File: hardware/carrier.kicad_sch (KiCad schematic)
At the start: 49 parts, among them J2 Heltec_J2, J3 Heltec_J3, U2 TCA9534PWR, U3 NS4168

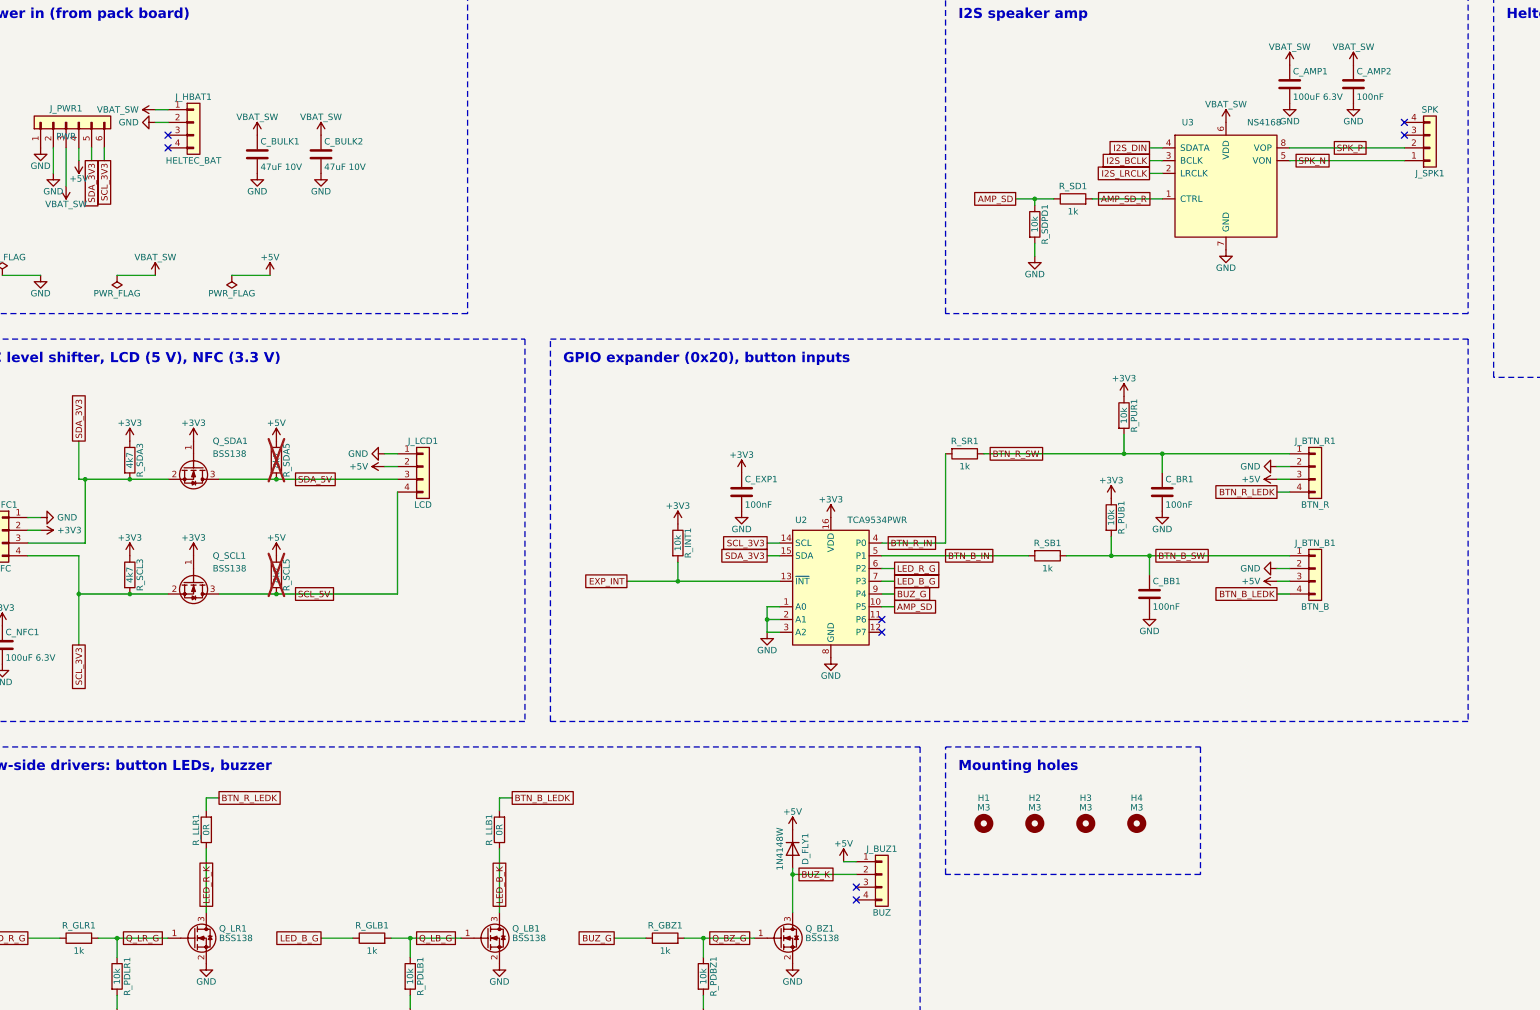
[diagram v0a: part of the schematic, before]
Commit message: hardware: off-board 2-wire connectors back to XH-2
J_HBAT1, J_BUZ1 and J_SPK1 (carrier) and J_KEY1 (pack) go back to JST-XH B2B-XH-A (C158012) instead of 4-pin B4B-XH-A (C144395) with pins 3-4 left no-connect. XH_SPARE is gone from both boards; the freed width puts J_BTN_R1 back on the carrier's top edge. Regenerated: both boards ERC/DRC clean, 0 unrouted.
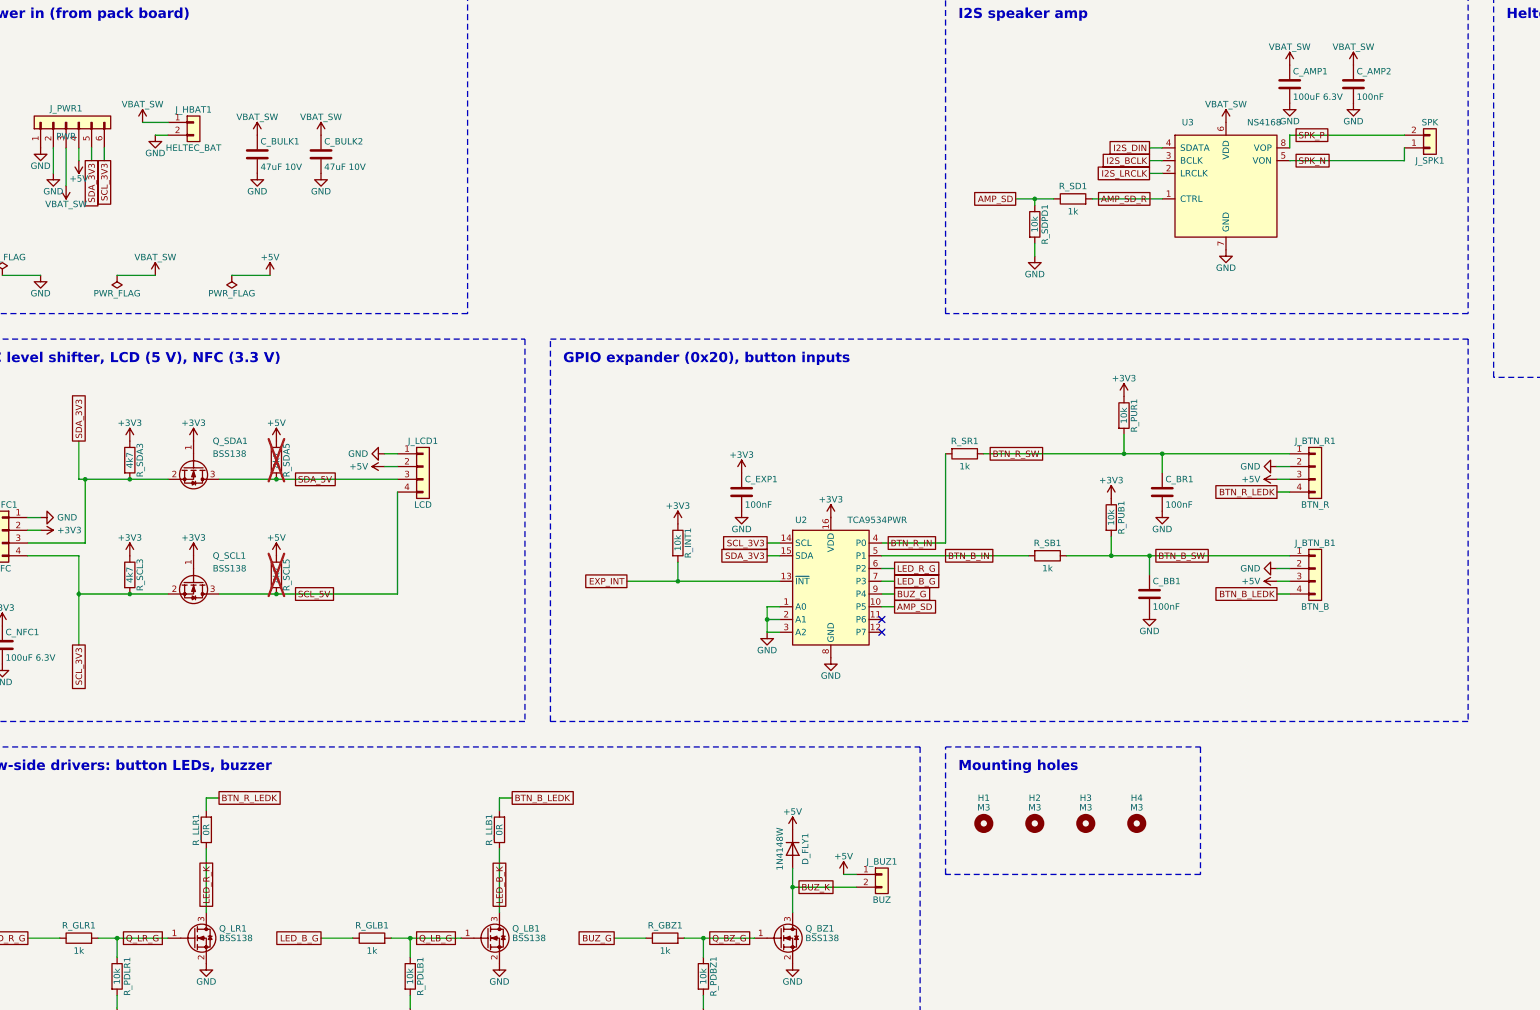
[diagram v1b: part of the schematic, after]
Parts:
- J_BUZ1, J_HBAT1, J_SPK1: footprint Connector_JST:JST_XH_B4B-XH-A_1x04_P2.50mm_Vertical -> Connector_JST:JST_XH_B2B-XH-A_1x02_P2.50mm_Vertical; symbol Connector_Generic:Conn_01x04 -> Connector_Generic:Conn_01x02
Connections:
- no-connect marks 34 -> 28
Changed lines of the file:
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@@
 	(wire
 		(pts
-			(xy 187.96 185.42)
-			(xy 190.5 185.42)
+			(xy 187.96 187.96)
+			(xy 190.5 187.96)
 		)
 		(stroke
@@
 	(wire
 		(pts
-			(xy 177.8 187.96)
-			(xy 190.5 187.96)
+			(xy 177.8 190.5)
+			(xy 190.5 190.5)
 		)
 		(stroke
@@
 		(pts
 			(xy 177.8 186.69)
-			(xy 177.8 187.96)
+			(xy 177.8 190.5)
 		)
 		(stroke
@@
 	(wire
 		(pts
-			(xy 177.8 187.96)
+			(xy 177.8 190.5)
 			(xy 177.8 195.58)
 		)
@@
 	)
 	(junction
-		(at 177.8 187.96)
+		(at 177.8 190.5)
 		(diameter 0)
 		(color 0 0 0 0)
@@
 	(wire
 		(pts
-			(xy 50.8 38.1)
-			(xy 53.34 38.1)
+			(xy 50.8 40.64)
+			(xy 53.34 40.64)
 		)
 		(stroke
@@
 	(wire
 		(pts
-			(xy 276.86 43.18)
 			(xy 299.72 43.18)
+			(xy 299.72 45.72)
 		)
 		(stroke
@@
 	(wire
 		(pts
-			(xy 50.8 35.56)
-			(xy 53.34 35.56)
+			(xy 276.86 40.64)
+			(xy 299.72 40.64)
+		)
+		(stroke
+			(width 0)
+			(type default)
+		)
+	)
+	(wire
+		(pts
+			(xy 276.86 40.64)
+			(xy 276.86 43.18)
+		)
+		(stroke
+			(width 0)
+			(type default)
+		)
+	)
+	(wire
+		(pts
+			(xy 48.26 38.1)
+			(xy 53.34 38.1)
 		)
 		(stroke
@@
 		)
 	)
-	(no_connect
-		(at 53.34 40.64)
-	)
-	(no_connect
-		(at 53.34 43.18)
-	)
 	(rectangle
 		(start 208.28 12.7)
@@
 		)
 	)
-	(no_connect
-		(at 299.72 40.64)
-	)
-	(no_connect
-		(at 299.72 38.1)
-	)
 	(rectangle
 		(start 317.5 12.7)
@@
 		)
 	)
-	(no_connect
-		(at 190.5 190.5)
-	)
-	(no_connect
-		(at 190.5 193.04)
-	)
 	(rectangle
 		(start 208.28 162.56)
@@
 	(global_label "SPK_P"
 		(shape passive)
-		(at 285.75 43.18 0)
+		(at 278.13 40.64 0)
 		(fields_autoplaced yes)
 		(effects
@@
 	(global_label "BUZ_K"
 		(shape passive)
-		(at 179.07 187.96 0)
+		(at 179.07 190.5 0)
 		(fields_autoplaced yes)
 		(effects
@@
 	)
 	(symbol
-		(lib_id "Connector_Generic:Conn_01x04")
+		(lib_id "Connector_Generic:Conn_01x02")
 		(at 58.42 38.1 0)
 		(unit 1)
@@
 		(dnp no)
 		(property "Reference" "J_HBAT1"
-			(at 58.42 33.02 0)
+			(at 58.42 35.56 0)
 			(effects
 				(font
@@
 		)
 		(property "Value" "HELTEC_BAT"
-			(at 58.42 45.72 0)
+			(at 58.42 43.18 0)
 			(effects
 				(font
@@
 			)
 		)
-		(property "Footprint" "Connector_JST:JST_XH_B4B-XH-A_1x04_P2.50mm_Vertical"
+		(property "Footprint" "Connector_JST:JST_XH_B2B-XH-A_1x02_P2.50mm_Vertical"
 			(at 58.42 38.1 0)
 			(effects
@@
 			)
 		)
-		(property "Description" "Generic connector, single row, 01x04, script generated (kicad-library-utils/schlib/autogen/connector/)"
+		(property "Description" "Generic connector, single row, 01x02, script generated (kicad-library-utils/schlib/autogen/connector/)"
 			(at 58.42 38.1 0)
 			(effects
@@
 		(pin "2"
 		)
-		(pin "3"
-		)
-		(pin "4"
-		)
 		(instances
 			(project "carrier"
@@
 	)
 	(symbol
-		(lib_id "Connector_Generic:Conn_01x04")
+		(lib_id "Connector_Generic:Conn_01x02")
 		(at 304.8 43.18 0)
 		(mirror x)
@@
 		(dnp no)
 		(property "Reference" "J_SPK1"
-			(at 304.8 48.26 0)
+			(at 304.8 45.72 0)
 			(effects
 				(font
@@
 		)
 		(property "Value" "SPK"
-			(at 304.8 35.56 0)
+			(at 304.8 38.1 0)
 			(effects
 				(font
@@
 			)
 		)
-		(property "Footprint" "Connector_JST:JST_XH_B4B-XH-A_1x04_P2.50mm_Vertical"
+		(property "Footprint" "Connector_JST:JST_XH_B2B-XH-A_1x02_P2.50mm_Vertical"
 			(at 304.8 43.18 0)
 			(effects
@@
 			)
 		)
-		(property "Description" "Generic connector, single row, 01x04, script generated (kicad-library-utils/schlib/autogen/connector/)"
+		(property "Description" "Generic connector, single row, 01x02, script generated (kicad-library-utils/schlib/autogen/connector/)"
 			(at 304.8 43.18 0)
 			(effects
@@
 		(pin "2"
 		)
-		(pin "3"
-		)
-		(pin "4"
-		)
 		(instances
 			(project "carrier"
@@
 	)
 	(symbol
-		(lib_id "Connector_Generic:Conn_01x04")
+		(lib_id "Connector_Generic:Conn_01x02")
 		(at 195.58 187.96 0)
 		(unit 1)
@@
 		(dnp no)
 		(property "Reference" "J_BUZ1"
-			(at 195.58 182.88 0)
+			(at 195.58 185.42 0)
 			(effects
 				(font
@@
 		)
 		(property "Value" "BUZ"
-			(at 195.58 195.58 0)
+			(at 195.58 193.04 0)
 			(effects
 				(font
@@
 			)
 		)
-		(property "Footprint" "Connector_JST:JST_XH_B4B-XH-A_1x04_P2.50mm_Vertical"
+		(property "Footprint" "Connector_JST:JST_XH_B2B-XH-A_1x02_P2.50mm_Vertical"
 			(at 195.58 187.96 0)
 			(effects
@@
 			)
 		)
-		(property "Description" "Generic connector, single row, 01x04, script generated (kicad-library-utils/schlib/autogen/connector/)"
+		(property "Description" "Generic connector, single row, 01x02, script generated (kicad-library-utils/schlib/autogen/connector/)"
 			(at 195.58 187.96 0)
 			(effects
@@
 		(pin "2"
 		)
-		(pin "3"
-		)
-		(pin "4"
-		)
 		(instances
 			(project "carrier"
@@
 	(symbol
 		(lib_id "power:GND")
-		(at 50.8 38.1 270)
+		(at 50.8 40.64 0)
 		(unit 1)
 		(exclude_from_sim no)
@@
 		(dnp no)
 		(property "Reference" "#PWR05"
-			(at 50.8 38.1 0)
+			(at 50.8 40.64 0)
 			(effects
 				(font
@@
 		)
 		(property "Value" "GND"
-			(at 47.5 38.1 90)
+			(at 50.8 44.24 0)
 			(effects
 				(font
 					(size 1.27 1.27)
 				)
-				(justify right)
 			)
 		)
 		(property "Footprint" ""
-			(at 50.8 38.1 0)
+			(at 50.8 40.64 0)
 			(effects
 				(font
@@
 		)
 		(property "Datasheet" ""
-			(at 50.8 38.1 0)
+			(at 50.8 40.64 0)
 			(effects
 				(font
@@
 		)
 		(property "Description" ""
-			(at 50.8 38.1 0)
+			(at 50.8 40.64 0)
 			(effects
 				(font
@@
 	(symbol
 		(lib_id "power:+5V")
-		(at 187.96 185.42 0)
+		(at 187.96 187.96 0)
 		(unit 1)
 		(exclude_from_sim no)
@@
 		(dnp no)
 		(property "Reference" "#PWR52"
-			(at 187.96 185.42 0)
+			(at 187.96 187.96 0)
 			(effects
 				(font
@@
 		)
 		(property "Value" "+5V"
-			(at 187.96 181.82 0)
+			(at 187.96 184.36 0)
 			(effects
 				(font
@@
 		)
 		(property "Footprint" ""
-			(at 187.96 185.42 0)
+			(at 187.96 187.96 0)
 			(effects
 				(font
@@
 		)
 		(property "Datasheet" ""
-			(at 187.96 185.42 0)
+			(at 187.96 187.96 0)
 			(effects
 				(font
@@
 		)
 		(property "Description" ""
-			(at 187.96 185.42 0)
+			(at 187.96 187.96 0)
 			(effects
 				(font
@@
 	(symbol
 		(lib_id "power:+BATT")
-		(at 50.8 35.56 90)
+		(at 48.26 38.1 0)
 		(unit 1)
 		(exclude_from_sim no)
@@
 		(dnp no)
 		(property "Reference" "#PWR53"
-			(at 50.8 35.56 0)
+			(at 48.26 38.1 0)
 			(effects
 				(font
@@
 		)
 		(property "Value" "VBAT_SW"
-			(at 47.5 35.56 270)
+			(at 48.26 34.5 0)
 			(effects
 				(font
 					(size 1.27 1.27)
 				)
-				(justify right)
 			)
 		)
 		(property "Footprint" ""
-			(at 50.8 35.56 0)
+			(at 48.26 38.1 0)
 			(effects
 				(font
@@
 		)
 		(property "Datasheet" ""
-			(at 50.8 35.56 0)
+			(at 48.26 38.1 0)
 			(effects
 				(font
@@
 		)
 		(property "Description" ""
-			(at 50.8 35.56 0)
+			(at 48.26 38.1 0)
 			(effects
 				(font
